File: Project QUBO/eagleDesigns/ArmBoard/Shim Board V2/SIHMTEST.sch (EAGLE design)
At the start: 14 parts, among them IC1 MCP2551/SN, U1 BME280

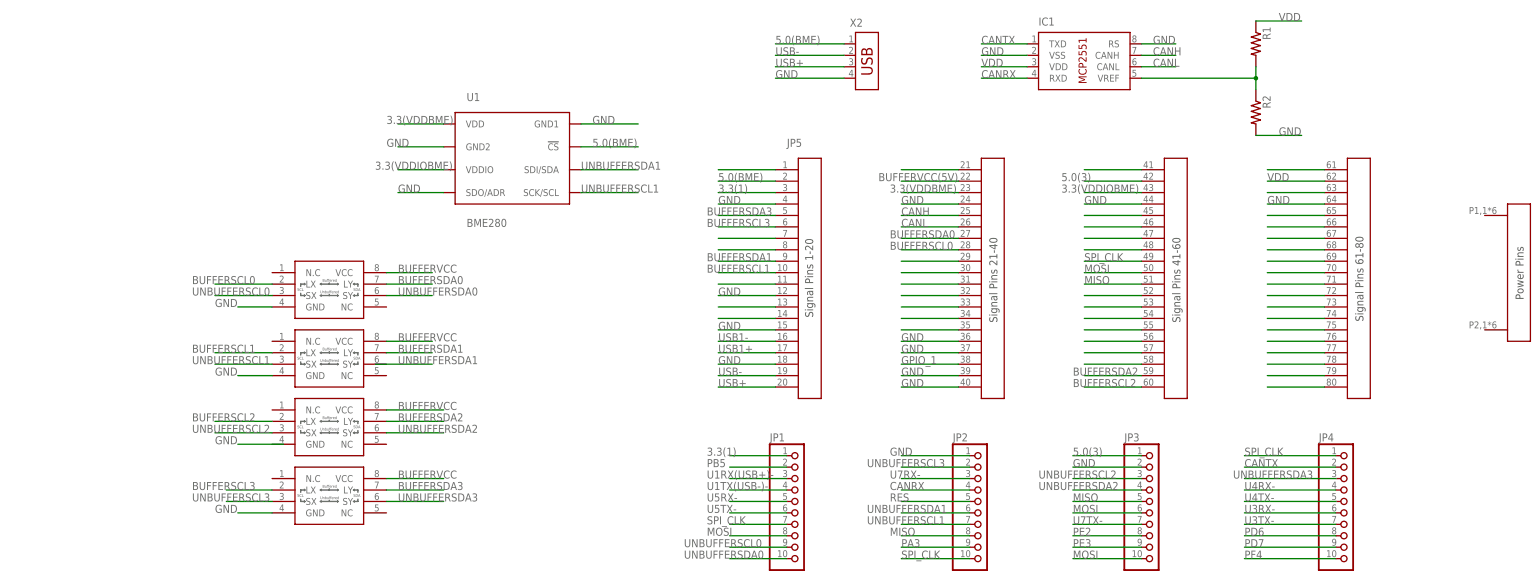
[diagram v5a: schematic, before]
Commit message: 
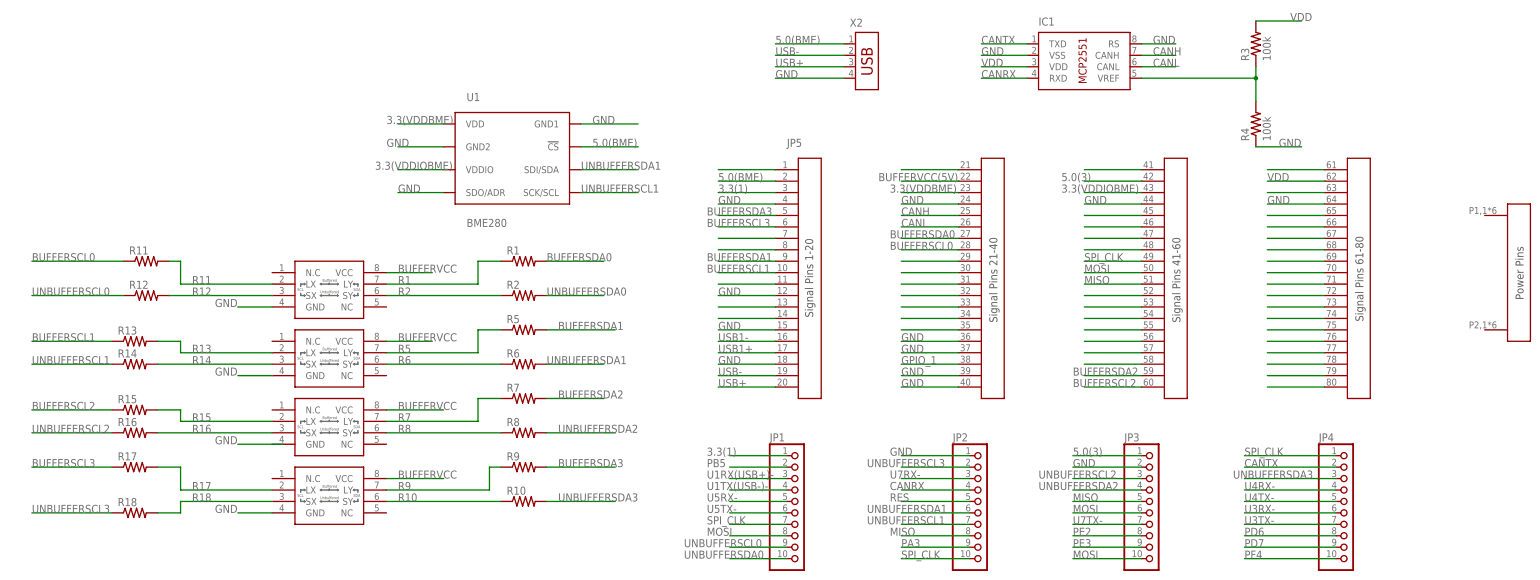
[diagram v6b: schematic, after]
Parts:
- added R10, R11, R12, R13, R14, R15, R16, R17, R18, R5, R6, R7, R8, R9: (no value), resistor:R-US_R0805
- added R3, R4: 100k, resistor:R-US_R0805
- R1, R2: device resistor:R-US_0204/2V -> resistor:R-US_R0805
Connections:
- new net R1: R1.1, U$1.LY
- new net R10: R10.1, U$4.SY
- new net R11: R11.2, U$1.LX
- new net R12: R12.2, U$1.SX
- new net R13: R13.2, U$2.LX
- new net R14: R14.2, U$2.SX
- new net R15: R15.2, U$3.LX
- new net R16: R16.2, U$3.SX
- new net R17: R17.2, U$4.LX
- new net R18: R18.2, U$4.SX
- new net R2: R2.1, U$1.SY
- new net R5: R5.1, U$2.LY
- new net R6: R6.1, U$2.SY
- new net R7: R7.1, U$3.LY
- new net R8: R8.1, U$3.SY
- new net R9: R9.1, U$4.LY
- net BUFFERSCL0: now also R11.1; no longer U$1.LX
- net BUFFERSCL1: now also R13.1; no longer U$2.LX
- net BUFFERSCL2: now also R15.1; no longer U$3.LX
- net BUFFERSCL3: now also R17.1; no longer U$4.LX
- net BUFFERSDA0: now also R1.2; no longer U$1.LY
- net BUFFERSDA1: now also R5.2; no longer U$2.LY
- net BUFFERSDA2: now also R7.2; no longer U$3.LY
- net BUFFERSDA3: now also R9.2; no longer U$4.LY
- net GND: now also R4.1; no longer R2.2
- net N$2: now also R3.1, R4.2; no longer R1.2, R2.1
- net UNBUFFERSCL0: now also R12.1; no longer U$1.SX
- net UNBUFFERSCL1: now also R14.1; no longer U$2.SX
- net UNBUFFERSCL2: now also R16.1; no longer U$3.SX
- net UNBUFFERSCL3: now also R18.1; no longer U$4.SX
- net UNBUFFERSDA0: now also R2.2; no longer U$1.SY
- net UNBUFFERSDA1: now also R6.2
- net UNBUFFERSDA2: now also R8.2; no longer U$3.SY
- net UNBUFFERSDA3: now also R10.2; no longer U$4.SY
- net VDD: now also R3.2; no longer R1.1
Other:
- moved on the sheet: R1, R2

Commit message: 
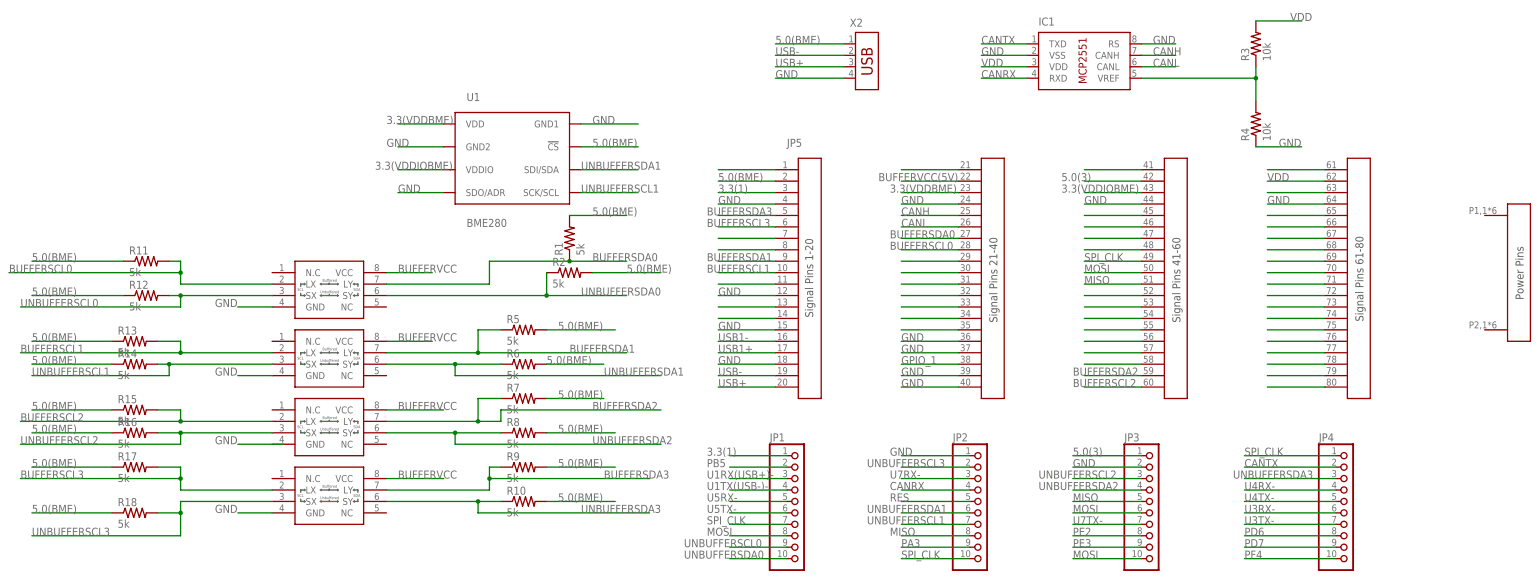
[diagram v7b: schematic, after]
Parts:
- R1, R10, R11, R12, R13, R14, R15, R16, R17, R18, R2, R5, R6, R7, R8, R9: value (none) -> 5k
- R3, R4: value 100k -> 10k
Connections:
- removed net R1: R1.1, U$1.LY
- removed net R10: R10.1, U$4.SY
- removed net R11: R11.2, U$1.LX
- removed net R12: R12.2, U$1.SX
- removed net R13: R13.2, U$2.LX
- removed net R14: R14.2, U$2.SX
- removed net R15: R15.2, U$3.LX
- removed net R16: R16.2, U$3.SX
- removed net R17: R17.2, U$4.LX
- removed net R18: R18.2, U$4.SX
- removed net R2: R2.1, U$1.SY
- removed net R5: R5.1, U$2.LY
- removed net R6: R6.1, U$2.SY
- removed net R7: R7.1, U$3.LY
- removed net R8: R8.1, U$3.SY
- removed net R9: R9.1, U$4.LY
- net 5.0(BME): now also R1.2, R10.2, R11.1, R12.1, R13.1, R14.1, R15.1, R16.1, R17.1, R18.1, R2.2, R5.2, R6.2, R7.2, R8.2, R9.2
- net BUFFERSCL0: now also R11.2, U$1.LX; no longer R11.1
- net BUFFERSCL1: now also R13.2, U$2.LX; no longer R13.1
- net BUFFERSCL2: now also R15.2, U$3.LX; no longer R15.1
- net BUFFERSCL3: now also R17.2, U$4.LX; no longer R17.1
- net BUFFERSDA0: now also R1.1, U$1.LY; no longer R1.2
- net BUFFERSDA1: now also R5.1, U$2.LY; no longer R5.2
- net BUFFERSDA2: now also R7.1, U$3.LY; no longer R7.2
- net BUFFERSDA3: now also R9.1, U$4.LY; no longer R9.2
- net UNBUFFERSCL0: now also R12.2, U$1.SX; no longer R12.1
- net UNBUFFERSCL1: now also R14.2, U$2.SX; no longer R14.1
- net UNBUFFERSCL2: now also R16.2, U$3.SX; no longer R16.1
- net UNBUFFERSCL3: now also R18.2, U$4.SX; no longer R18.1
- net UNBUFFERSDA0: now also R2.1, U$1.SY; no longer R2.2
- net UNBUFFERSDA1: now also R6.1, U$2.SY; no longer R6.2
- net UNBUFFERSDA2: now also R8.1, U$3.SY; no longer R8.2
- net UNBUFFERSDA3: now also R10.1, U$4.SY; no longer R10.2
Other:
- moved on the sheet: R1, R2
